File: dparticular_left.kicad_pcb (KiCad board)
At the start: 2 copper layers, 185.7 x 157.2 mm, 51 parts, among them J2 Outside USB, J3 To Right Hand, J4 Teensy USB, SW1 Reset, SW1:6 Key_Scrl, SW1:7 Key_Paus, SW2:1 Key_ESC, SW2:2 Key_F1, SW2:3 Key_F2, SW2:4 Key_F3, SW2:5 Key_F4, SW2:6 Key_F5, SW2:7 Key_F6, SW3:1 Key_Home, SW3:2 Key_End, SW3:3 Key_Tilde, SW3:4 Key_1, SW3:5 Key_2, SW3:6 Key_3, SW3:7 Key_4, SW3:8 Key_5, SW4:2 Key_PgUp, SW4:3 Key_Tab, SW4:4 Key_Q, SW4:5 Key_W, SW4:6 Key_E, SW4:7 Key_R, SW4:8 Key_T, SW5:2 Key_PgDn, SW5:3 Key_Caps, SW5:4 Key_A, SW5:5 Key_S, SW5:6 Key_D, SW5:7 Key_F, SW5:8 Key_G, SW6:3 Key_LShft, SW6:4 Key_Z, SW6:5 Key_X, SW6:6 Key_C, SW6:7 Key_V, SW6:8 Key_B, SW7:3 Key_LCtrl, SW7:4 Key_Fn, SW7:5 Key_LWin, SW7:6 Key_LAlt, SW7:8 Key_LSpc, U2 TEENSY2.0

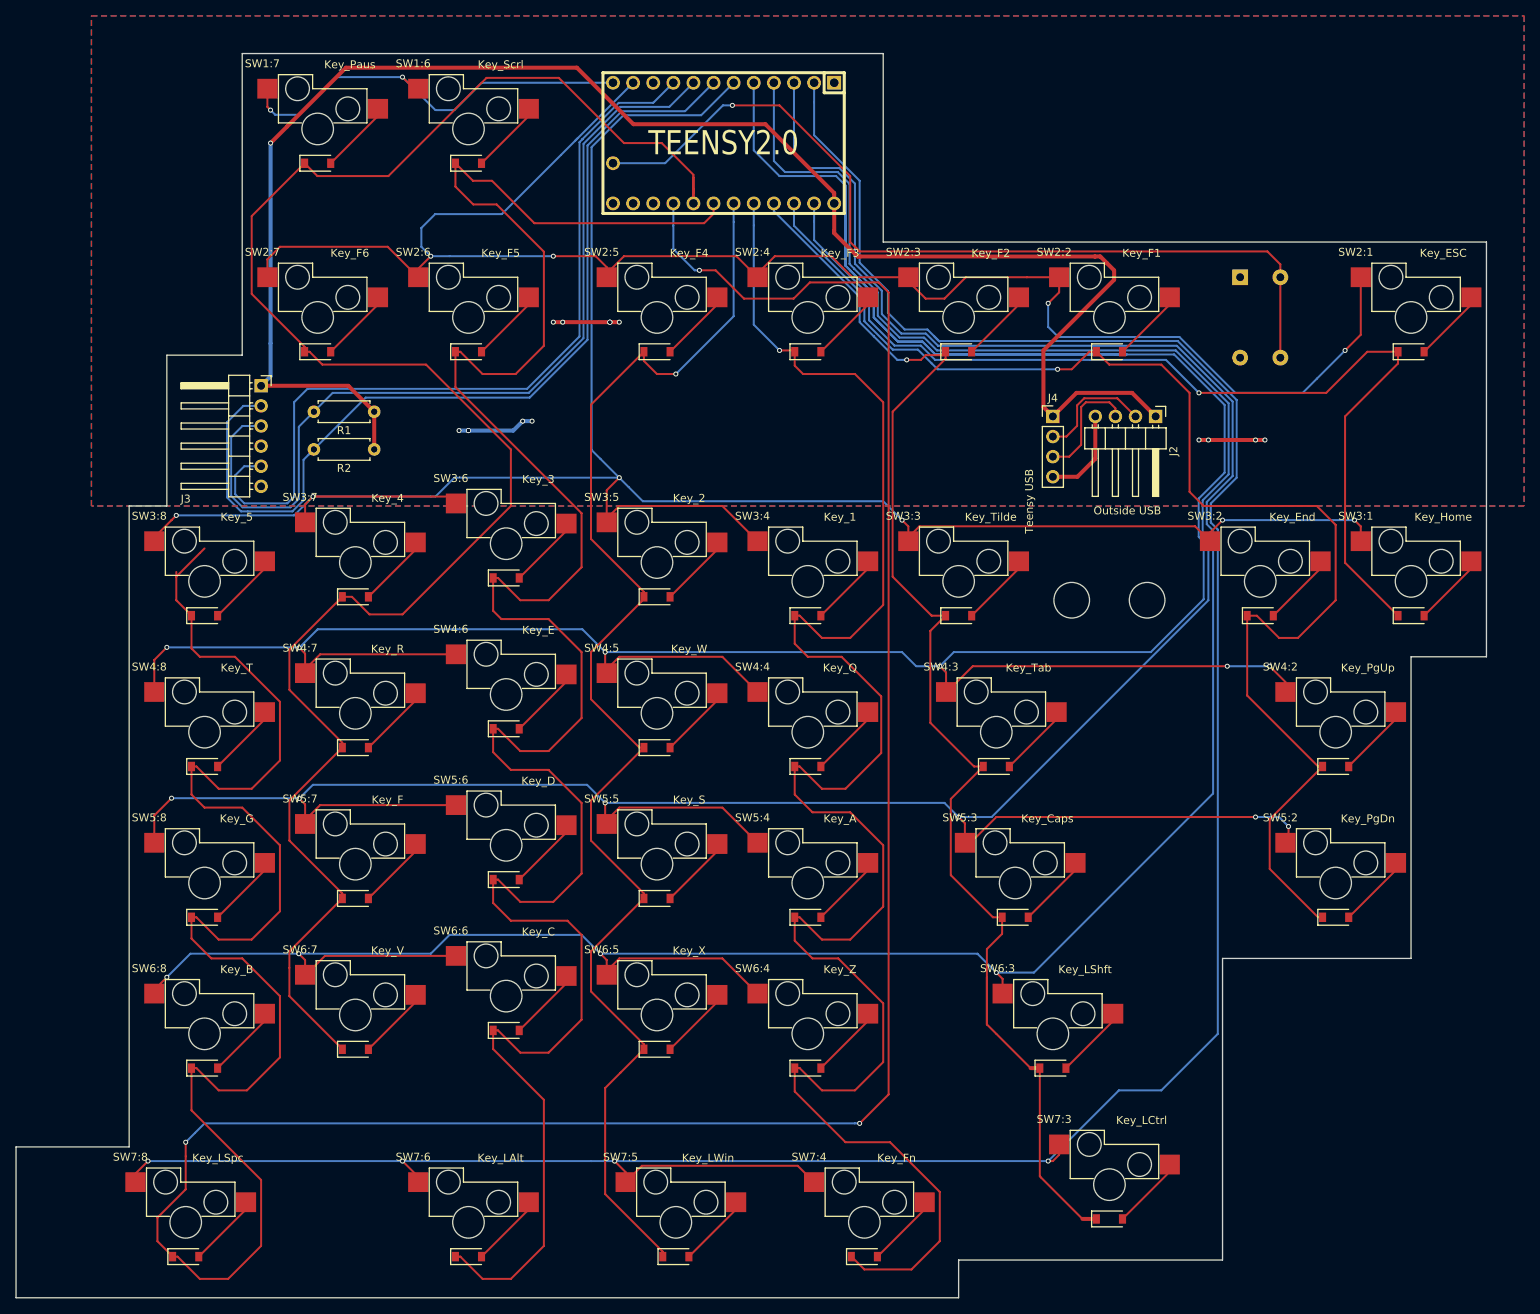
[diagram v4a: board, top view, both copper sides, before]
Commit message: PCBs: Clean up via line by line analysis
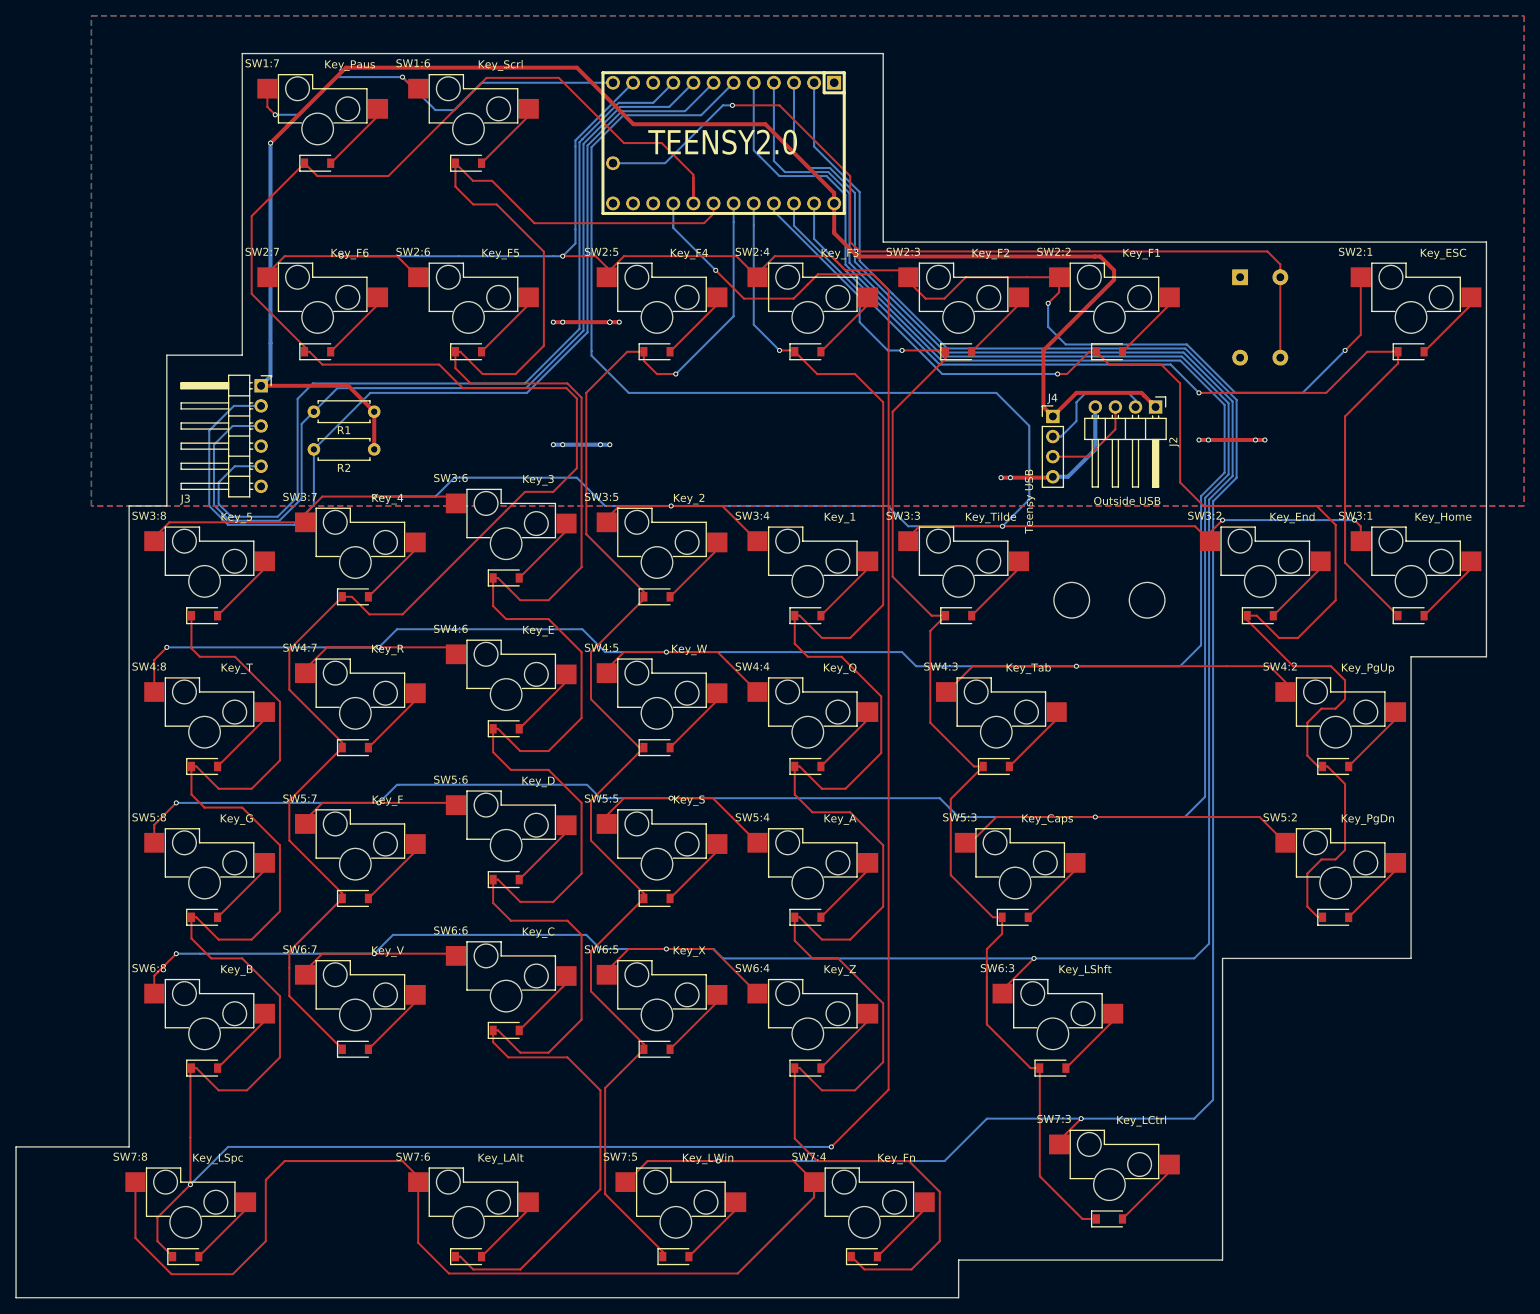
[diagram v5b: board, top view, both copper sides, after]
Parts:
- moved J2 1.19 mm to (163.0, 68.5)
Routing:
- net /ROW4: track 410.8 -> 348.8 mm, vias 6 -> 4
- net /ROW3: track 281.1 -> 330.2 mm, vias 6 -> 5
- net /ROW7: track 344.6 -> 387.4 mm, vias 4 -> 2
- net /COL8: track 415.3 -> 374.2 mm
- net /COL7: track 236.7 -> 254.4 mm
- net /COL6: track 292.6 -> 308.7 mm
- net /ROW2: track 214.4 -> 207.2 mm
- net /SCL: track 116.6 -> 123.1 mm
- net /COL2: track 170.0 -> 176.2 mm
- net /ROW6: track 335.6 -> 341.4 mm
- net /LED_D: track 105.3 -> 110.8 mm
- net /SDA: track 112.7 -> 118.2 mm
- net GND: track 38.0 -> 42.6 mm, vias 14 -> 15
- net /USB_DP: track 14.9 -> 12.1 mm
- net /COL4: track 238.7 -> 241.1 mm
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
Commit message: PCBs: Move vias off silk screen
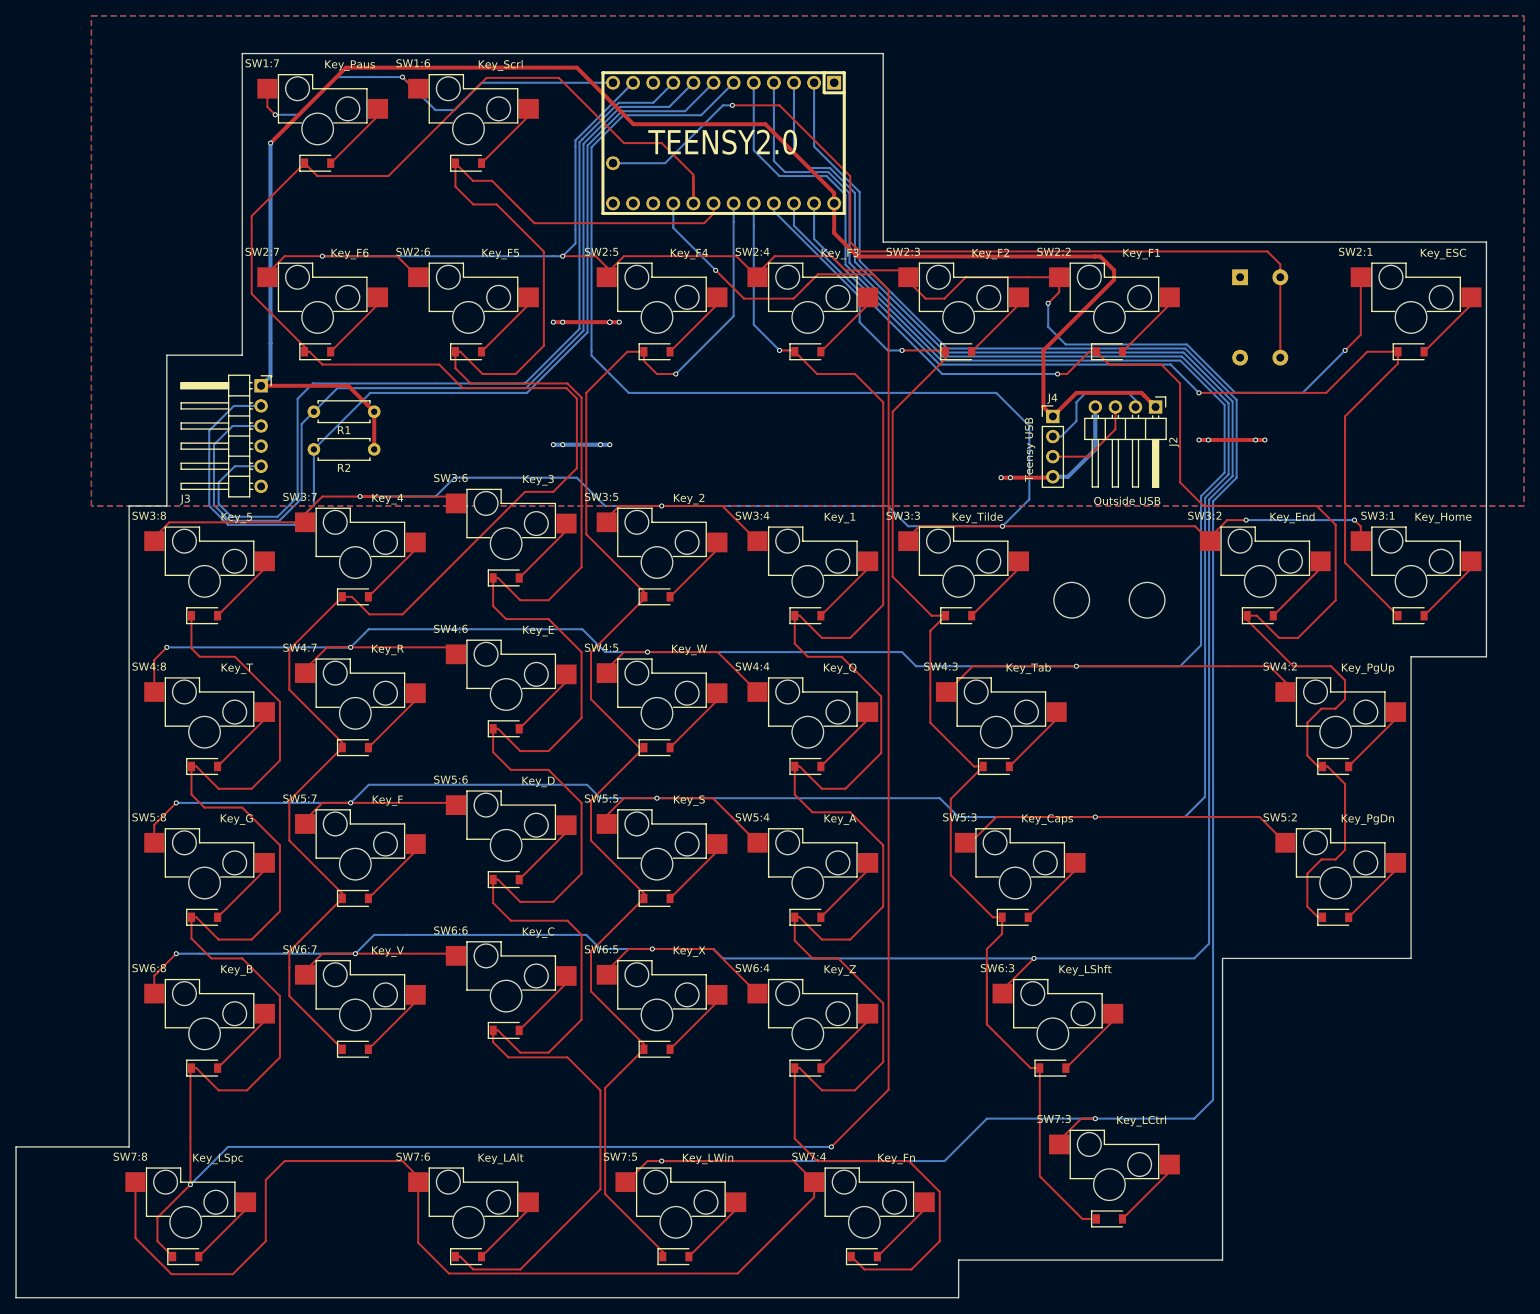
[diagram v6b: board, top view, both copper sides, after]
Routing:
- net /ROW7: track 387.4 -> 396.3 mm
- net /ROW6: track 341.4 -> 344.9 mm
- net /ROW3: track 330.2 -> 333.5 mm
- net /ROW2: track 207.2 -> 209.6 mm

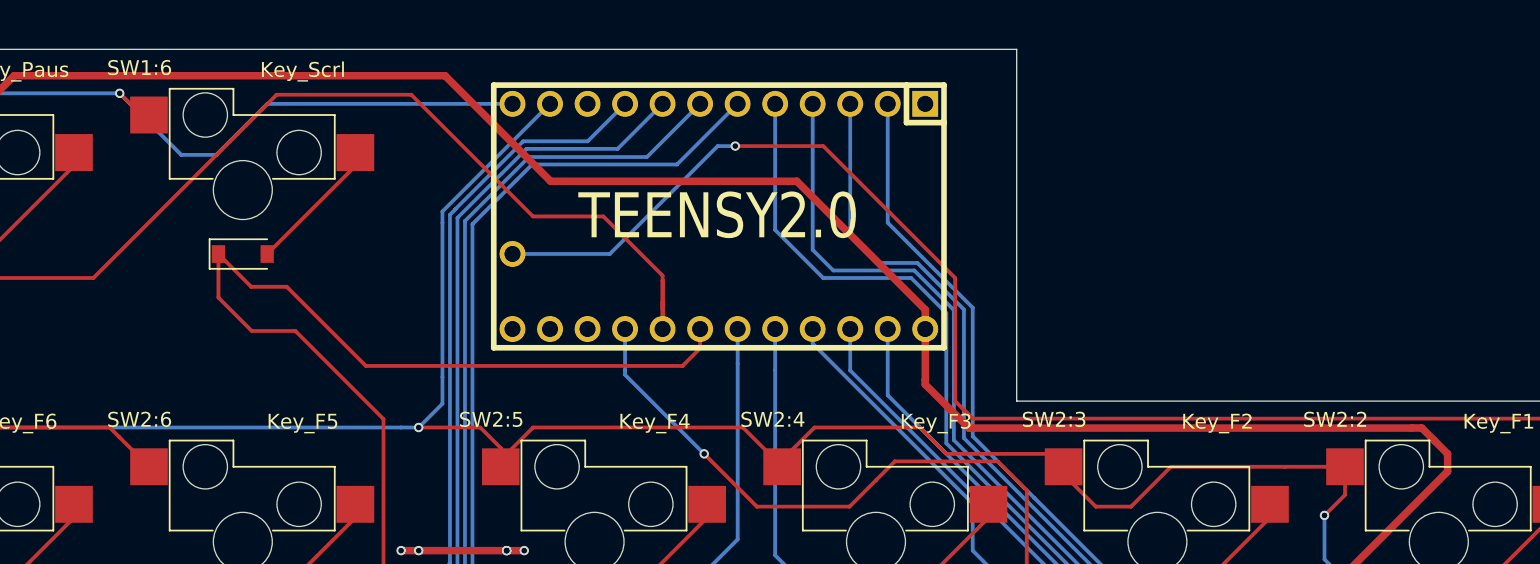
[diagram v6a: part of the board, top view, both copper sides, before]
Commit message: PCBs: More proofreading and cleanup
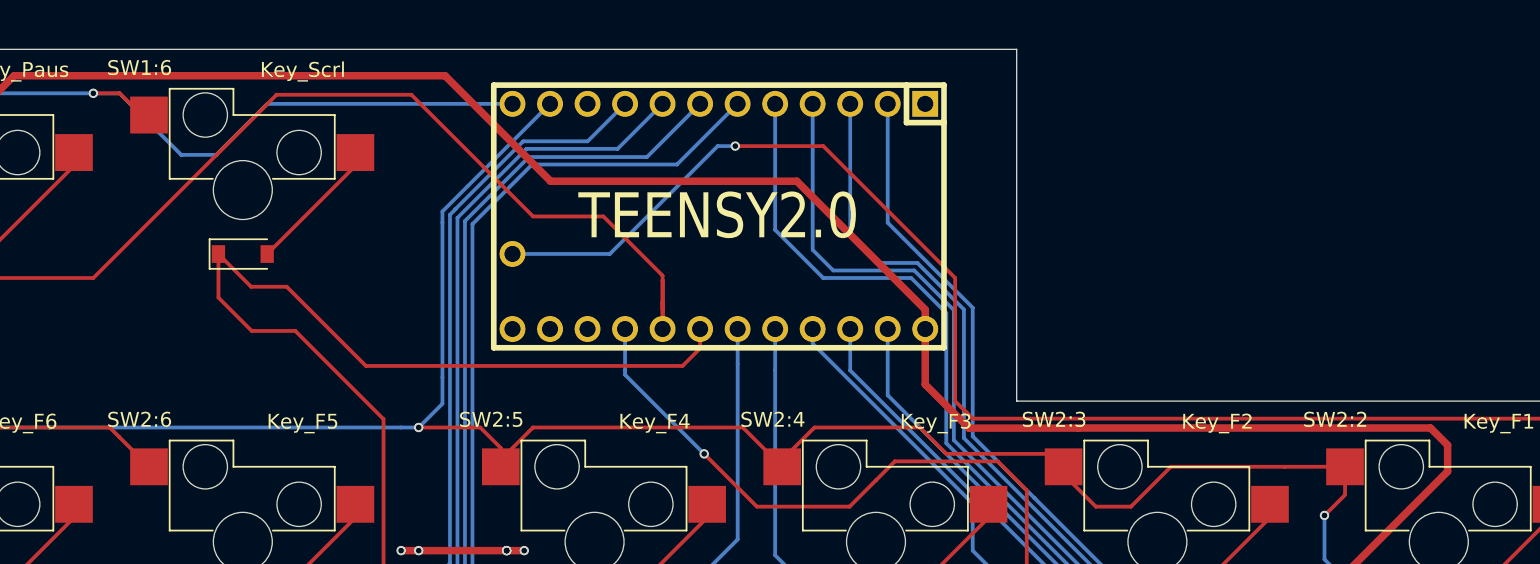
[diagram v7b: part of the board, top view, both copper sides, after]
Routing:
- net /ROW1: track 54.1 -> 55.9 mm

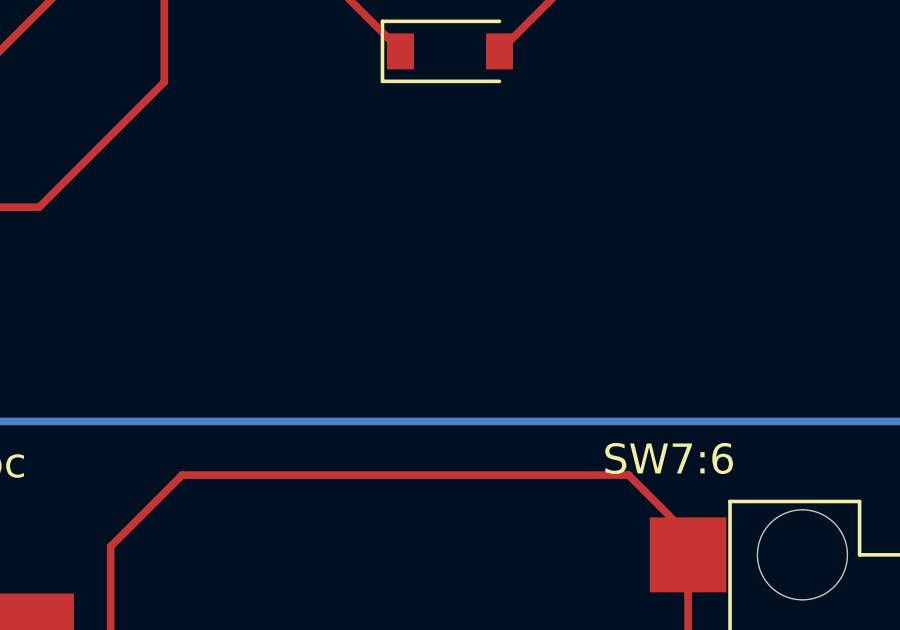
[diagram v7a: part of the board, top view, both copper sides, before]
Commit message: PCBs: Added JLC Order Number placeholders
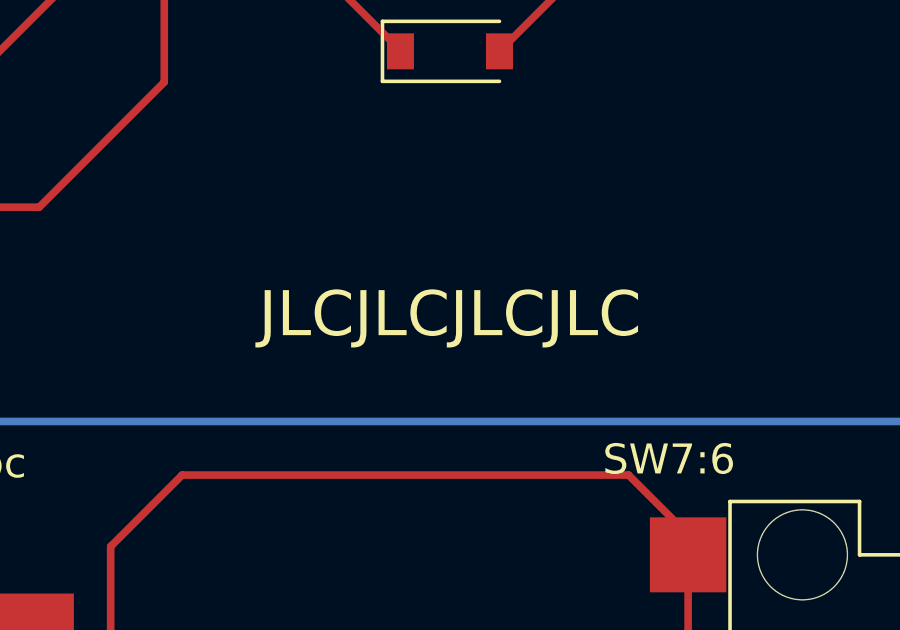
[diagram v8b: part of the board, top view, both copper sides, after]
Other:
- board text added: "JLCJLCJLCJLC"
